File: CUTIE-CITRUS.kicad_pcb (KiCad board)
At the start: 2 copper layers, 85 x 85 mm, 82 parts, among them J1 F32Q-1A7H1-11022, J2 F32Q-1A7H1-11022, J3 Bus_M.2_Socket_M, J4 Hirose U.FL, P1 ERM8-025-01-L-D-RA-K-TR, U1 AP3441SHE-7B, U2 ASEK-32.768KHZ-L-R-T, U3 ICM-42688-P, U4 NEO-M8M, U5 MCP98243, U6 MCP98243, U7 MCP2518FD-xQBB, U8 TCAN334

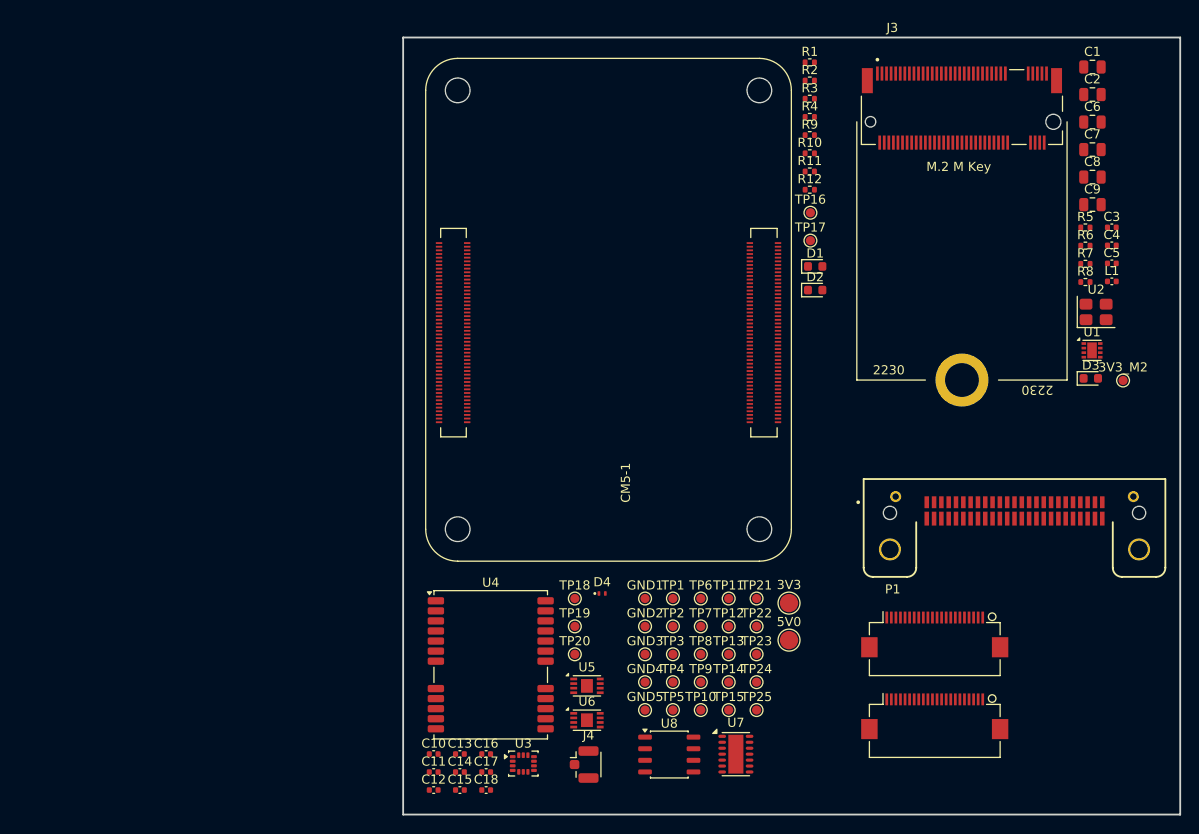
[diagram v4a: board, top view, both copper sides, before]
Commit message: removed ublox
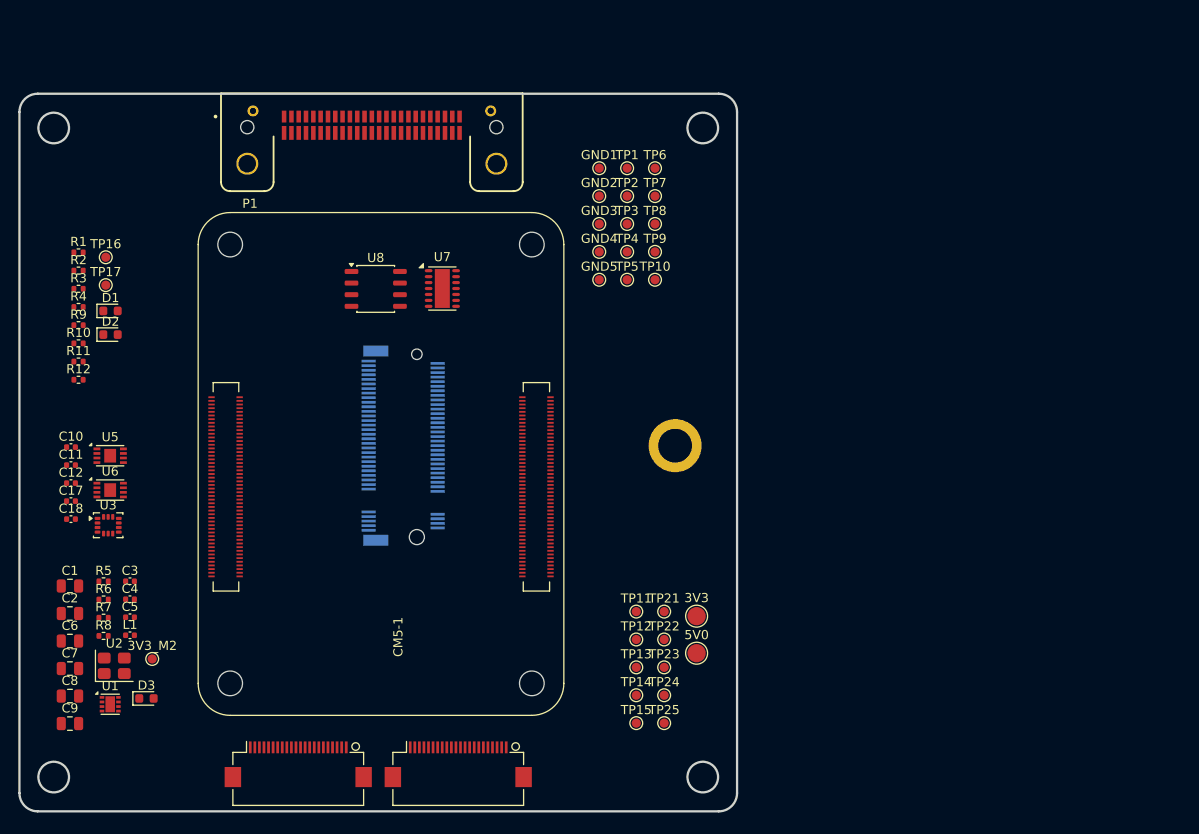
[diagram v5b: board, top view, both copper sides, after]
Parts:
- removed C13: 47pF, Capacitor_SMD:C_0402_1005Metric
- removed C14: 0.1uF, Capacitor_SMD:C_0402_1005Metric
- removed C15: 2.2uF, Capacitor_SMD:C_0402_1005Metric
- removed C16: 1uF, Capacitor_SMD:C_0402_1005Metric
- removed D4: TPD1E05U06DPY, Package_SON:Texas_DPY0002A_0.6x1mm_P0.65mm
- removed J4: Hirose U.FL, Connector_Coaxial:U.FL_Hirose_U.FL-R-SMT-1_Vertical
- removed TP18, TP19, TP20: TestPoint, TestPoint:TestPoint_Pad_D1.0mm
- removed U4: NEO-M8M, RF_GPS:ublox_NEO
- J3: moved to B.Cu
- moved C1 125.4 mm to (113.5, 110.0)
- moved C2 125.4 mm to (113.5, 113.0)
- moved C6 125.4 mm to (113.5, 116.0)
- moved C7 125.4 mm to (113.5, 119.0)
- moved C8 125.4 mm to (113.5, 122.0)
- moved C9 125.4 mm to (113.5, 125.0)
- moved C3 114.2 mm to (120.1, 109.5)
- moved C4 114.2 mm to (120.1, 111.5)
- moved C5 114.2 mm to (120.1, 113.4)
- moved U2 114.2 mm to (118.4, 118.7)
- moved R5 114.2 mm to (117.2, 109.5)
- moved R6 114.2 mm to (117.2, 111.5)
- moved R7 114.2 mm to (117.2, 113.5)
- moved R8 114.2 mm to (117.2, 115.5)
- moved U1 114.2 mm to (118.0, 122.9)
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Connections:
- net /CM5/GPIO/SPI4.CS0n renamed /CM5/SPI4.CS0n
- net /CM5/GPIO/SPI4.MISO renamed /CM5/SPI4.MISO
- net /CM5/GPIO/SPI4.MOSI renamed /CM5/SPI4.MOSI
- net /CM5/GPIO/SPI4.SCLK renamed /CM5/SPI4.SCLK
- net /CM5/SPI1.CS1n renamed /Backplane Connector/SPI1.CS1n
- TP21 pad 1: /CM5/SPI1.MISO -> /Backplane Connector/SPI1.MISO
- TP22 pad 1: /CM5/SPI1.MOSI -> /Backplane Connector/SPI1.MOSI
- TP23 pad 1: /CM5/SPI1.SCLK -> /Backplane Connector/SPI1.SCLK
- TP24 pad 1: /CM5/SPI1.CS0n -> /Backplane Connector/SPI1.CS0n
- U8 pad 6: unconnected-(U8-CANL-Pad6) -> /Backplane Connector/CAN0.L
- U8 pad 7: unconnected-(U8-CANH-Pad7) -> /Backplane Connector/CAN0.H
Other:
- board size 85 x 85 mm -> 78.5 x 78.5 mm
- board text added: "For Instructional Use Only."
- board text added: "SOLIDWORKS Educational Product."

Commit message: starting layout
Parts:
- removed TP22, TP23, TP24, TP25: TestPoint, TestPoint:TestPoint_Pad_D1.0mm
- added C13: 0.1uF, Capacitor_SMD:C_0402_1005Metric, F.Cu at (47.5, 38.5)
- added C14: 0.1uF, Capacitor_SMD:C_0402_1005Metric, F.Cu at (48.4, 42.8)
- added C15: 0.1uF, Capacitor_SMD:C_0402_1005Metric, F.Cu at (43.4, 49.8)
- added R13: 2.2K 1%, Resistor_SMD:R_0402_1005Metric, F.Cu at (44.1, 45.8)
- added TP18: TestPoint, TestPoint:TestPoint_Pad_D1.0mm, F.Cu at (97.8, 125.2)
- added TP19: TestPoint, TestPoint:TestPoint_Pad_D1.0mm, F.Cu at (97.8, 128.3)
- added TP20: TestPoint, TestPoint:TestPoint_Pad_D1.0mm, F.Cu at (97.8, 131.3)
- added Y1: ECS-2520MV-200-BN-TR, Oscillator:Oscillator_SMD_ECS_2520MV-xxx-xx-4Pin_2.5x2.0mm, F.Cu at (43.4, 47.8)
- CM5-1: moved to B.Cu
- J3: moved to F.Cu
- moved C1 124.4 mm to (234.3, 79.9)
- moved C2 124.4 mm to (234.3, 82.9)
- moved C6 124.4 mm to (234.3, 86.0)
- moved C7 124.4 mm to (234.3, 89.0)
- moved C8 124.4 mm to (234.3, 92.0)
- moved C9 124.4 mm to (234.3, 95.0)
- moved 3V3 121.9 mm to (61.3, 129.8)
- moved 5V0 121.9 mm to (61.3, 133.9)
- moved GND2 120.3 mm to (68.3, 129.3)
- moved GND1 120.3 mm to (68.3, 126.2)
- moved GND3 120.3 mm to (68.3, 132.3)
- moved GND4 120.3 mm to (68.3, 135.4)
- moved C3 116.9 mm to (236.4, 97.5)
- moved C4 116.9 mm to (236.4, 99.4)
- moved C5 116.9 mm to (236.4, 101.4)
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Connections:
- net Net-(U7-RXCAN) renamed /CM5/RXCAN
- net Net-(U7-TXCAN) renamed /CM5/TXCAN
- 3V3 pad 1: /Cameras/3V3 -> /CM5/3V3
- C10 pad 1: /Cameras/3V3 -> /CM5/3V3
- C11 pad 1: /Cameras/3V3 -> /CM5/3V3
- C12 pad 1: /Cameras/3V3 -> /CM5/3V3
- C17 pad 1: /Cameras/3V3 -> /CM5/3V3
- C18 pad 1: /Cameras/3V3 -> /CM5/3V3
- CM5-1 pad 128: unconnected-(CM5-1B-USB3-0-RX_N-Pad128) -> /Backplane Connector/USB3.RX_N
- CM5-1 pad 130: unconnected-(CM5-1B-USB3-0-RX_P-Pad130) -> /Backplane Connector/USB3.RX_P
- CM5-1 pad 134: unconnected-(CM5-1B-USB3-0-D_P-Pad134) -> /Backplane Connector/USB3.D_P
- CM5-1 pad 136: unconnected-(CM5-1B-USB3-0-D_N-Pad136) -> /Backplane Connector/USB3.D_N
- CM5-1 pad 140: unconnected-(CM5-1B-USB3-0-TX_N-Pad140) -> /Backplane Connector/USB3.TX_N
- CM5-1 pad 142: unconnected-(CM5-1B-USB3-0-TX_P-Pad142) -> /Backplane Connector/USB3.TX_P
- CM5-1 pad 157: /Backplane Connector/USB3.RX_N -> unconnected-(CM5-1B-USB3-1-RX_N-Pad157)
- CM5-1 pad 159: /Backplane Connector/USB3.RX_P -> unconnected-(CM5-1B-USB3-1-RX_P-Pad159)
- CM5-1 pad 163: /Backplane Connector/USB3.D_P -> unconnected-(CM5-1B-USB3-1-D_P-Pad163)
- CM5-1 pad 165: /Backplane Connector/USB3.D_N -> unconnected-(CM5-1B-USB3-1-D_N-Pad165)
- CM5-1 pad 169: /Backplane Connector/USB3.TX_N -> unconnected-(CM5-1B-USB3-1-TX_N-Pad169)
- CM5-1 pad 171: /Backplane Connector/USB3.TX_P -> unconnected-(CM5-1B-USB3-1-TX_P-Pad171)
- CM5-1 pad 194: GND -> /CM5/DPHY1.D3_N
- CM5-1 pad 196: GND -> /CM5/DPHY1.D3_P
- CM5-1 pad 25: unconnected-(CM5-1A-GPIO21-Pad25) -> /CM5/SPI1.SCLK
- CM5-1 pad 26: unconnected-(CM5-1A-GPIO19-Pad26) -> /CM5/SPI1.MISO
- CM5-1 pad 27: unconnected-(CM5-1A-GPIO20-Pad27) -> /CM5/SPI1.MOSI
- CM5-1 pad 28: unconnected-(CM5-1A-GPIO13-Pad28) -> /CM5/I2C2.SDA
- CM5-1 pad 30: unconnected-(CM5-1A-GPIO6-Pad30) -> /CM5/GPIO/SPI3.MOSI
- CM5-1 pad 31: unconnected-(CM5-1A-GPIO12-Pad31) -> /CM5/I2C2.SDA
- CM5-1 pad 34: /CM5/I2C2.SCL -> /CM5/GPIO/SPI3.MISO
- CM5-1 pad 35: /CM5/I2C1.SCL -> /Backplane Connector/SPI2.MISO
- CM5-1 pad 36: /CM5/I2C1.SDA -> /Backplane Connector/SPI2.CS0n
- CM5-1 pad 37: /CM5/SPI0.CS1n -> /CM5/GPIO/SPI3.SCLK
- CM5-1 pad 38: /CM5/SPI0.SCLK -> /CM5/I2C1.SCL
- CM5-1 pad 39: /CM5/SPI0.CS0n -> /CM5/I2C0.SDA
- CM5-1 pad 40: /CM5/SPI0.MISO -> /CM5/I2C0.SCL
- CM5-1 pad 41: unconnected-(CM5-1A-GPIO25-Pad41) -> /CM5/CAN_INT
- CM5-1 pad 44: /CM5/SPI0.MOSI -> /CM5/I2C1.SDA
- CM5-1 pad 49: unconnected-(CM5-1A-GPIO18-Pad49) -> /CM5/SPI1.CS0n
- CM5-1 pad 50: unconnected-(CM5-1A-GPIO17-Pad50) -> /CM5/SPI1.CS1n
- CM5-1 pad 54: /CM5/I2C2.SDA -> /CM5/GPIO/SPI3.CS0n
- CM5-1 pad 56: unconnected-(CM5-1A-GPIO3-Pad56) -> /Backplane Connector/SPI2.SCLK
- CM5-1 pad 58: unconnected-(CM5-1A-GPIO2-Pad58) -> /Backplane Connector/SPI2.MOSI
- CM5-1 pad 78: /Cameras/3V3 -> /CM5/3V3
- CM5-1 pad 80: /CM5/I2C0.SCL -> unconnected-(CM5-1A-GPIO39-Pad80)
- CM5-1 pad 82: /CM5/I2C0.SDA -> unconnected-(CM5-1A-GPIO38-Pad82)
- CM5-1 pad 84: /Cameras/3V3 -> /CM5/3V3
- CM5-1 pad 86: /Cameras/3V3 -> /CM5/3V3
- D1 pad 2: /Cameras/3V3 -> /CM5/3V3
- D2 pad 2: /Cameras/3V3 -> /CM5/3V3
- J1 pad 22: /Cameras/3V3 -> /CM5/3V3
- J2 pad 22: /Cameras/3V3 -> /CM5/3V3
- P1 pad 01: (no net) -> /Backplane Connector/CAN0.L
- P1 pad 02: (no net) -> GND
- P1 pad 03: (no net) -> /Backplane Connector/CAN0.H
- P1 pad 04: (no net) -> GND
- P1 pad 05: (no net) -> GND
- P1 pad 06: (no net) -> /Backplane Connector/USB3.D_N
- P1 pad 07: (no net) -> GND
- P1 pad 08: (no net) -> /Backplane Connector/USB3.D_P
- P1 pad 09: (no net) -> unconnected-(P1-Pad09)
- P1 pad 30: /Backplane Connector/SPI1.MOSI -> /Backplane Connector/SPI2.MOSI
- P1 pad 32: /Backplane Connector/SPI1.MISO -> /Backplane Connector/SPI2.MISO
- P1 pad 38: /Backplane Connector/SPI1.SCLK -> /Backplane Connector/SPI2.SCLK
- P1 pad 40: /Backplane Connector/SPI1.CS0n -> /Backplane Connector/SPI2.CS0n
- R1 pad 1: /Cameras/3V3 -> /CM5/3V3
- R10 pad 1: /Cameras/3V3 -> /CM5/3V3
- R11 pad 1: /Cameras/3V3 -> /CM5/3V3
- R12 pad 1: /Cameras/3V3 -> /CM5/3V3
- R2 pad 1: /Cameras/3V3 -> /CM5/3V3
- R9 pad 1: /Cameras/3V3 -> /CM5/3V3
- TP1 pad 1: /CM5/SPI0.MISO -> /CM5/PCIEsb.nCLKREQ
- TP10 pad 1: /CM5/I2C2.SDA -> /CM5/I2C2.SCL
- TP11 pad 1: /CM5/I2C2.SCL -> /CM5/SPI1.MISO
- TP12 pad 1: /CM5/PCIEsb.nCLKREQ -> /CM5/SPI1.MOSI
- TP13 pad 1: /CM5/PCIEsb.nWAKE -> /CM5/SPI1.SCLK
- TP14 pad 1: /CM5/PCIEsb.PWR_EN -> /CM5/SPI1.CS0n
- TP15 pad 1: /CM5/PCIEsb.nRST -> /CM5/SPI1.CS1n
- TP2 pad 1: /CM5/SPI0.MOSI -> /CM5/PCIEsb.nWAKE
- TP21 pad 1: /Backplane Connector/SPI1.MISO -> /Backplane Connector/SPI2.CS0n
- TP3 pad 1: /CM5/SPI0.SCLK -> /CM5/PCIEsb.PWR_EN
- TP4 pad 1: /CM5/SPI0.CS0n -> /CM5/PCIEsb.nRST
- TP5 pad 1: /CM5/SPI0.CS1n -> /CM5/I2C0.SDA
- TP6 pad 1: /CM5/I2C0.SDA -> /CM5/I2C0.SCL
- TP7 pad 1: /CM5/I2C0.SCL -> /CM5/I2C1.SDA
- TP8 pad 1: /CM5/I2C1.SDA -> /CM5/I2C1.SCL
- TP9 pad 1: /CM5/I2C1.SCL -> /CM5/I2C2.SDA
- U3 pad 1: /CM5/SPI0.MISO -> /CM5/SPI1.MISO
- U3 pad 12: /CM5/SPI0.CS0n -> /CM5/SPI1.CS0n
- U3 pad 13: /CM5/SPI0.SCLK -> /CM5/SPI1.SCLK
- U3 pad 14: /CM5/SPI0.MOSI -> /CM5/SPI1.MOSI
- U3 pad 5: /Cameras/3V3 -> /CM5/3V3
- U3 pad 8: /Cameras/3V3 -> /CM5/3V3
- U5 pad 8: /Cameras/3V3 -> /CM5/3V3
- U6 pad 1: /Cameras/3V3 -> /CM5/3V3
- U6 pad 8: /Cameras/3V3 -> /CM5/3V3
- U7 pad 10: /CM5/SPI4.SCLK -> /CM5/GPIO/SPI3.SCLK
- U7 pad 11: /CM5/SPI4.MOSI -> /CM5/GPIO/SPI3.MOSI
- U7 pad 12: /CM5/SPI4.MISO -> /CM5/GPIO/SPI3.MISO
- U7 pad 13: /CM5/SPI4.CS0n -> /CM5/GPIO/SPI3.CS0n
- U7 pad 14: unconnected-(U7-VDD-Pad14) -> /CM5/3V3
- U7 pad 15: unconnected-(U7-VSS-Pad15) -> GND
- U7 pad 4: unconnected-(U7-~{INT}-Pad4) -> /CM5/CAN_INT
- U7 pad 6: unconnected-(U7-OSC1-Pad6) -> /CM5/OSC1
- U7 pad 7: unconnected-(U7-VSS-Pad7) -> GND
- U8 pad 2: unconnected-(U8-GND-Pad2) -> GND
- U8 pad 3: unconnected-(U8-VCC-Pad3) -> /CM5/3V3
- U8 pad 5: unconnected-(U8-SHDN-Pad5) -> GND
- U8 pad 8: unconnected-(U8-STB-Pad8) -> /CM5/3V3
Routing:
- added copper zone on B.Cu, net GND
- added copper zone on F.Cu, net GND
- added copper zone on In1.Cu, net GND
- added copper zone on In2.Cu, net GND
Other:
- copper layers 2 -> 4
- board text removed: "For Instructional Use Only."
- board text removed: "SOLIDWORKS Educational Product."

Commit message: high-speed signals initial
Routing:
- net /CM5/DPHY1.D0_P: track 0.00 -> 73.9 mm, vias 0 -> 1
- net /CM5/DPHY1.D0_N: track 0.00 -> 73.9 mm, vias 0 -> 1
- net /CM5/DPHY1.D2_P: track 0.00 -> 73.2 mm, vias 0 -> 1
- net /CM5/DPHY1.D2_N: track 0.00 -> 73.2 mm, vias 0 -> 1
- net /CM5/DPHY1.C_P: track 0.00 -> 72.7 mm, vias 0 -> 1
- net /CM5/DPHY1.C_N: track 0.00 -> 72.7 mm, vias 0 -> 1
- net /CM5/DPHY1.D1_P: track 0.00 -> 72.6 mm, vias 0 -> 1
- net /CM5/DPHY1.D1_N: track 0.00 -> 72.6 mm, vias 0 -> 1
- net /CM5/DPHY1.D3_P: track 0.00 -> 72.0 mm, vias 0 -> 1
- net /CM5/DPHY1.D3_N: track 0.00 -> 72.0 mm, vias 0 -> 1
- net /Backplane Connector/USB3.D_P: track 0.00 -> 62.4 mm, vias 0 -> 1
- net /Backplane Connector/USB3.D_N: track 0.00 -> 60.9 mm, vias 0 -> 1
- net /Backplane Connector/USB3.RX_N: track 0.00 -> 59.6 mm, vias 0 -> 1
- net /Backplane Connector/USB3.RX_P: track 0.00 -> 59.6 mm, vias 0 -> 1
- net /Backplane Connector/USB3.TX_N: track 0.00 -> 59.6 mm, vias 0 -> 1
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- removed copper zone on In1.Cu, net GND
- removed copper zone on In2.Cu, net GND

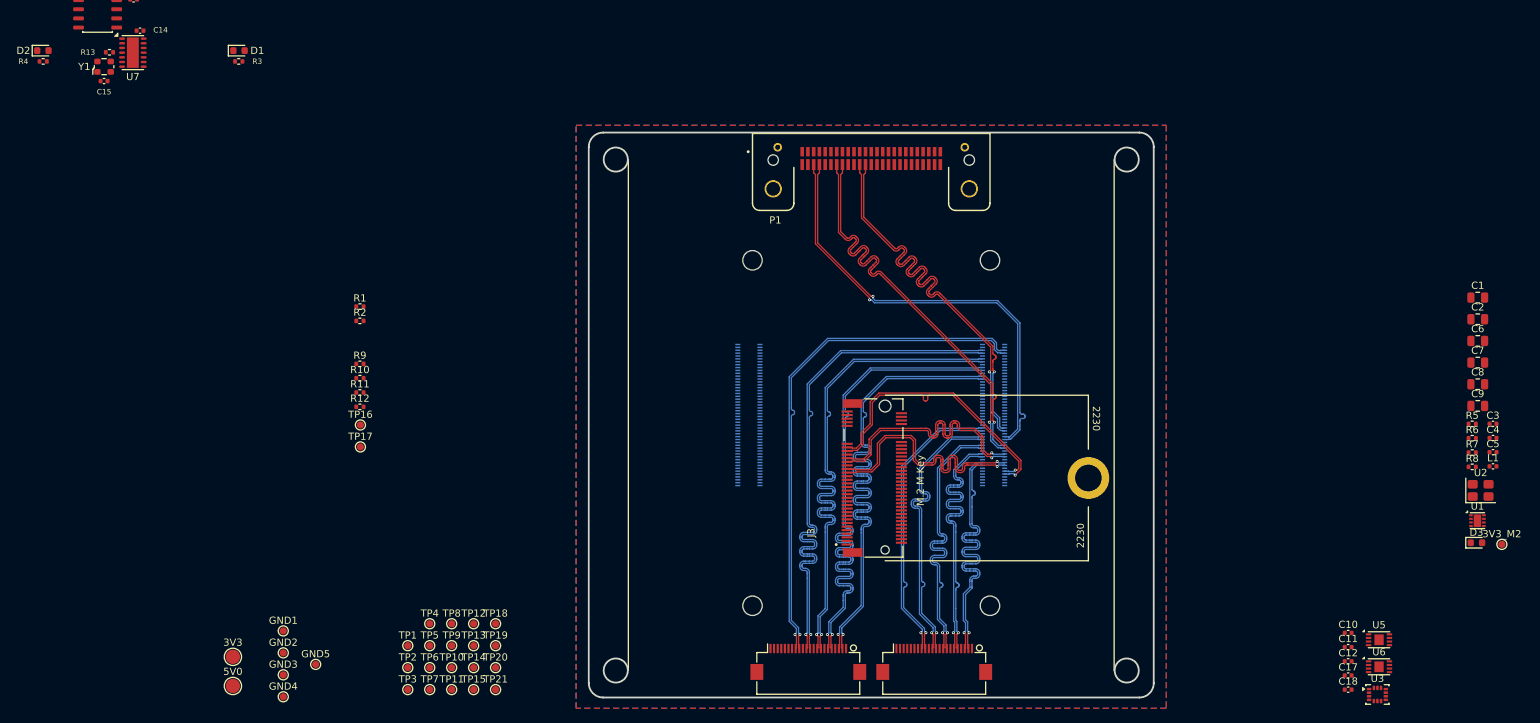
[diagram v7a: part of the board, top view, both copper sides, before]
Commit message: 3v3_m2 and 5v0 power planes
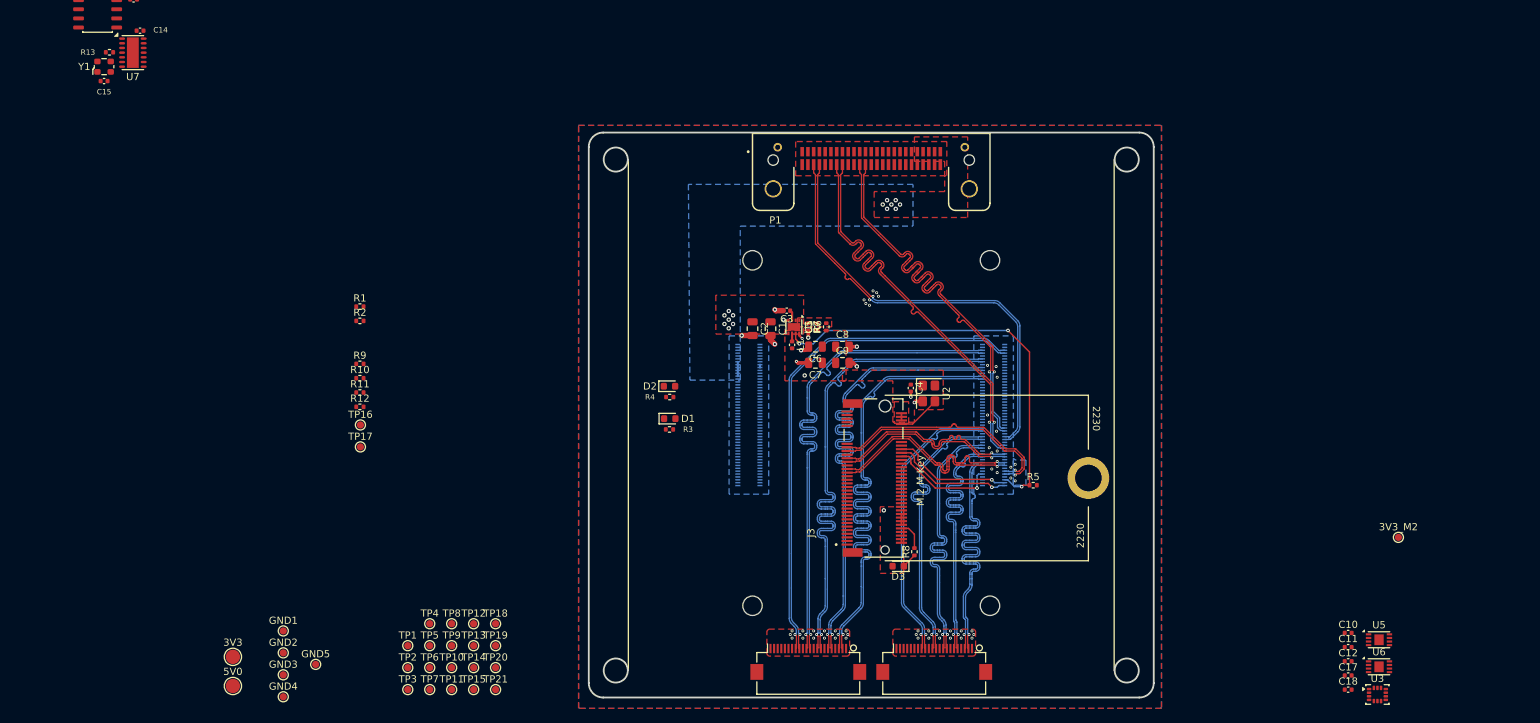
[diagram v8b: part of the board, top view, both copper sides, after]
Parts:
- moved C2 100.8 mm to (133.5, 84.2), turned to -90 degrees
- moved C3 99.4 mm to (138.2, 81.8), turned to 180 degrees
- moved L1 98.8 mm to (139.0, 86.5), turned to -90 degrees
- moved D2 98.8 mm to (122.0, 92.2)
- moved R4 98.8 mm to (122.0, 93.8)
- moved U1 98.7 mm to (139.2, 84.0), turned to -90 degrees
- moved C1 98.4 mm to (136.0, 84.2), turned to -90 degrees
- moved C5 95.5 mm to (142.5, 84.0), turned to 90 degrees
- moved R7 93.9 mm to (141.2, 84.0), turned to -90 degrees
- moved C6 92.0 mm to (142.2, 86.8), turned to 180 degrees
- moved C7 92.0 mm to (142.2, 89.0), turned to 180 degrees
- moved R6 91.1 mm to (143.8, 84.0), turned to 90 degrees
- moved C9 88.5 mm to (146.0, 89.0)
- moved C8 88.4 mm to (146.0, 86.8)
- moved C4 81.2 mm to (155.5, 92.5), turned to -90 degrees
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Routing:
- net /CM5/PCIEsb.PWR_EN: track 0.00 -> 58.1 mm, vias 0 -> 3
- net /NVME/3V3_M2: track 0.00 -> 31.5 mm, vias 0 -> 2
- net /CM5/PCIEsb.nCLKREQ: track 0.00 -> 16.9 mm, vias 0 -> 1
- net /CM5/PCIEsb.nWAKE: track 0.00 -> 16.7 mm, vias 0 -> 1
- net /CM5/PCIEsb.nRST: track 0.00 -> 15.3 mm, vias 0 -> 1
- net GND: track 0.00 -> 14.1 mm, vias 0 -> 59
- net /CM5/PCIE.TX_P: track 34.0 -> 26.0 mm
- net /CM5/PCIE.TX_N: track 34.0 -> 27.5 mm
- net /CM5/PCIE.CLK_N: track 37.9 -> 31.3 mm
- net /CM5/PCIE.RX_P: track 35.3 -> 28.9 mm
- net /NVME/SUSCLK: track 0.00 -> 5.99 mm
- net /CM5/PCIE.CLK_P: track 37.9 -> 32.9 mm
- net /CM5/PCIE.RX_N: track 35.3 -> 30.4 mm
- net /NVME/nLED1: track 0.00 -> 4.06 mm
- net /Backplane Connector/5V0: track 0.00 -> 3.46 mm, vias 0 -> 14
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- added copper zone on B.Cu, net /Backplane Connector/5V0
- added copper zone on F.Cu, net /Backplane Connector/5V0
- added copper zone on F.Cu, net /NVME/3V3_M2
- added copper zone on F.Cu, net /NVME/FB
- added copper zone on In1.Cu, net GND
- added copper zone on In2.Cu, net GND
